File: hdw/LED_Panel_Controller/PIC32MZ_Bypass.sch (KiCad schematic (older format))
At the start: 14 parts

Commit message: added digikey pns, footprints, bom scrubbed
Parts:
- C? (x6): Digi-Key PN 490-13211-1-ND -> 1276-1451-1-ND
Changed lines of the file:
@@
 F 5 "6.3V" H 3090 3400 50  0000 R CNN "Voltage"
 F 6 "X5R" H 3090 3300 50  0000 R CNN "Dielectric"
-F 7 "490-13211-1-ND" H 3240 3400 50  0001 C CNN "Digi-Key PN"
+F 7 "1276-1451-1-ND" H 3240 3400 50  0001 C CNN "Digi-Key PN"
 	1    3240 3400
 	1    0    0    -1
@@
 F 5 "6.3V" H 4390 3400 50  0000 R CNN "Voltage"
 F 6 "X5R" H 4390 3300 50  0000 R CNN "Dielectric"
-F 7 "490-13211-1-ND" H 4540 3400 50  0001 C CNN "Digi-Key PN"
+F 7 "1276-1451-1-ND" H 4540 3400 50  0001 C CNN "Digi-Key PN"
 	1    4540 3400
 	1    0    0    -1
@@
 F 5 "6.3V" H 6990 3400 50  0000 R CNN "Voltage"
 F 6 "X5R" H 6990 3300 50  0000 R CNN "Dielectric"
-F 7 "490-13211-1-ND" H 7140 3400 50  0001 C CNN "Digi-Key PN"
+F 7 "1276-1451-1-ND" H 7140 3400 50  0001 C CNN "Digi-Key PN"
 	1    7140 3400
 	1    0    0    -1
@@
 F 5 "6.3V" H 5690 3400 50  0000 R CNN "Voltage"
 F 6 "X5R" H 5690 3300 50  0000 R CNN "Dielectric"
-F 7 "490-13211-1-ND" H 5840 3400 50  0001 C CNN "Digi-Key PN"
+F 7 "1276-1451-1-ND" H 5840 3400 50  0001 C CNN "Digi-Key PN"
 	1    5840 3400
 	1    0    0    -1
@@
 F 5 "6.3V" H 3090 4400 50  0000 R CNN "Voltage"
 F 6 "X5R" H 3090 4300 50  0000 R CNN "Dielectric"
-F 7 "490-13211-1-ND" H 3240 4400 50  0001 C CNN "Digi-Key PN"
+F 7 "1276-1451-1-ND" H 3240 4400 50  0001 C CNN "Digi-Key PN"
 	1    3240 4400
 	1    0    0    -1
@@
 F 5 "6.3V" H 6990 4400 50  0000 R CNN "Voltage"
 F 6 "X5R" H 6990 4300 50  0000 R CNN "Dielectric"
-F 7 "490-13211-1-ND" H 7140 4400 50  0001 C CNN "Digi-Key PN"
+F 7 "1276-1451-1-ND" H 7140 4400 50  0001 C CNN "Digi-Key PN"
 	1    7140 4400
 	1    0    0    -1

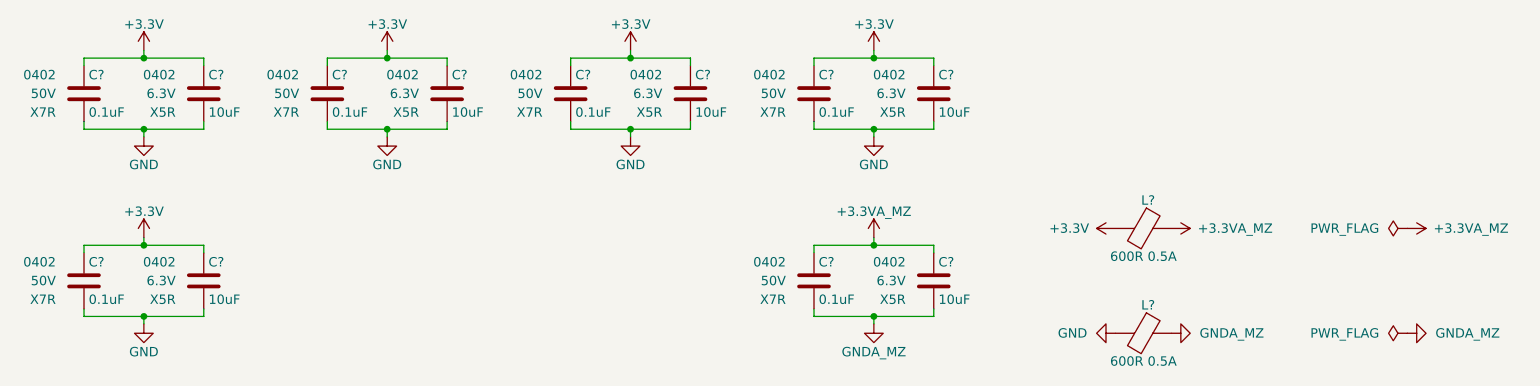
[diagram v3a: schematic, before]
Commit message: assigned I2C addresses
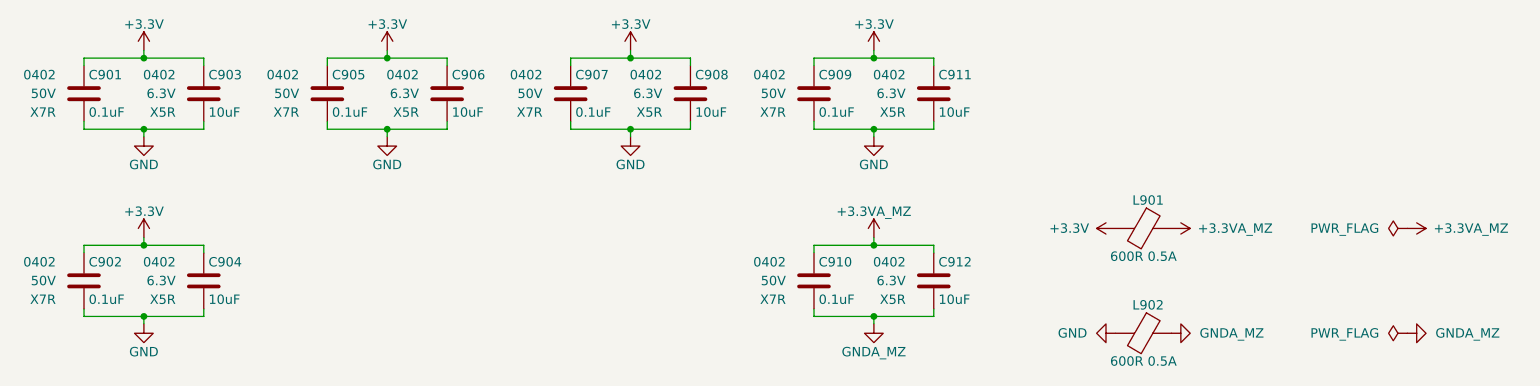
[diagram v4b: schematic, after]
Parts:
- gave numbers to parts that had none: 14
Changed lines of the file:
@@
 $EndDescr
 $Comp
-L Custom_Library:C_Custom C?
+L Custom_Library:C_Custom C901
 U 1 1 5CB29D37
 P 2600 3400
-F 0 "C?" H 2625 3500 50  0000 L CNN
+F 0 "C901" H 2625 3500 50  0000 L CNN
 F 1 "0.1uF" H 2625 3300 50  0000 L CNN
 F 2 "Capacitors_SMD:C_0402" H 2638 3250 50  0001 C CNN
@@
 	2600 3590 2600 3550
 $Comp
-L power:GND #PWR?
+L power:GND #PWR0906
 U 1 1 5CB1558B
 P 4220 3630
-F 0 "#PWR?" H 4220 3380 50  0001 C CNN
+F 0 "#PWR0906" H 4220 3380 50  0001 C CNN
 F 1 "GND" H 4220 3480 50  0000 C CNN
 F 2 "" H 4220 3630 50  0000 C CNN
@@
 $EndComp
 $Comp
-L Custom_Library:C_Custom C?
+L Custom_Library:C_Custom C905
 U 1 1 5CB15599
 P 3900 3400
-F 0 "C?" H 3925 3500 50  0000 L CNN
+F 0 "C905" H 3925 3500 50  0000 L CNN
 F 1 "0.1uF" H 3925 3300 50  0000 L CNN
 F 2 "Capacitors_SMD:C_0402" H 3938 3250 50  0001 C CNN
@@
 	4220 3590 4220 3630
 $Comp
-L power:GND #PWR?
+L power:GND #PWR0908
 U 1 1 5CB1993B
 P 5520 3630
-F 0 "#PWR?" H 5520 3380 50  0001 C CNN
+F 0 "#PWR0908" H 5520 3380 50  0001 C CNN
 F 1 "GND" H 5520 3480 50  0000 C CNN
 F 2 "" H 5520 3630 50  0000 C CNN
@@
 $EndComp
 $Comp
-L Custom_Library:C_Custom C?
+L Custom_Library:C_Custom C907
 U 1 1 5CB19945
 P 5200 3400
-F 0 "C?" H 5225 3500 50  0000 L CNN
+F 0 "C907" H 5225 3500 50  0000 L CNN
 F 1 "0.1uF" H 5225 3300 50  0000 L CNN
 F 2 "Capacitors_SMD:C_0402" H 5238 3250 50  0001 C CNN
@@
 	5520 3590 5520 3630
 $Comp
-L power:GND #PWR?
+L power:GND #PWR0910
 U 1 1 5CB219B2
 P 6820 3630
-F 0 "#PWR?" H 6820 3380 50  0001 C CNN
+F 0 "#PWR0910" H 6820 3380 50  0001 C CNN
 F 1 "GND" H 6820 3480 50  0000 C CNN
 F 2 "" H 6820 3630 50  0000 C CNN
@@
 $EndComp
 $Comp
-L Custom_Library:C_Custom C?
+L Custom_Library:C_Custom C909
 U 1 1 5CB219C0
 P 6500 3400
-F 0 "C?" H 6525 3500 50  0000 L CNN
+F 0 "C909" H 6525 3500 50  0000 L CNN
 F 1 "0.1uF" H 6525 3300 50  0000 L CNN
 F 2 "Capacitors_SMD:C_0402" H 6538 3250 50  0001 C CNN
@@
 	6820 3590 6820 3630
 $Comp
-L power:GND #PWR?
+L power:GND #PWR0904
 U 1 1 5CB24EB8
 P 2920 4630
-F 0 "#PWR?" H 2920 4380 50  0001 C CNN
+F 0 "#PWR0904" H 2920 4380 50  0001 C CNN
 F 1 "GND" H 2920 4480 50  0000 C CNN
 F 2 "" H 2920 4630 50  0000 C CNN
@@
 $EndComp
 $Comp
-L Custom_Library:C_Custom C?
+L Custom_Library:C_Custom C902
 U 1 1 5CB24EC6
 P 2600 4400
-F 0 "C?" H 2625 4500 50  0000 L CNN
+F 0 "C902" H 2625 4500 50  0000 L CNN
 F 1 "0.1uF" H 2625 4300 50  0000 L CNN
 F 2 "Capacitors_SMD:C_0402" H 2638 4250 50  0001 C CNN
@@
 	6500 4210 6500 4250
 $Comp
-L Custom_Library:C_Custom C?
+L Custom_Library:C_Custom C910
 U 1 1 5CB24FAA
 P 6500 4400
-F 0 "C?" H 6525 4500 50  0000 L CNN
+F 0 "C910" H 6525 4500 50  0000 L CNN
 F 1 "0.1uF" H 6525 4300 50  0000 L CNN
 F 2 "Capacitors_SMD:C_0402" H 6538 4250 50  0001 C CNN
@@
 AR Path="/5E697934/5CB5F840" Ref="L?"  Part="1"
 AR Path="/5EAE2F02/5CB5F840" Ref="L?"  Part="1"
-AR Path="/5F5829B3/5CB5F840" Ref="L?"  Part="1"
-F 0 "L?" V 8110 4145 50  0000 C CNN
+AR Path="/5F5829B3/5CB5F840" Ref="L901"  Part="1"
+F 0 "L901" V 8110 4145 50  0000 C CNN
 F 1 "600R 0.5A" V 8410 4120 50  0000 C CNN
 F 2 "Inductors_SMD:L_0402" V 8190 4120 50  0001 C CNN
@@
 AR Path="/5E697934/5CB61DC3" Ref="L?"  Part="1"
 AR Path="/5EAE2F02/5CB61DC3" Ref="L?"  Part="1"
-AR Path="/5F5829B3/5CB61DC3" Ref="L?"  Part="1"
-F 0 "L?" V 8110 4705 50  0000 C CNN
+AR Path="/5F5829B3/5CB61DC3" Ref="L902"  Part="1"
+F 0 "L902" V 8110 4705 50  0000 C CNN
 F 1 "600R 0.5A" V 8410 4680 50  0000 C CNN
 F 2 "Inductors_SMD:L_0402" V 8190 4680 50  0001 C CNN
@@
 $EndComp
 $Comp
-L power:GND #PWR?
+L power:GND #PWR0914
 U 1 1 5CB62D81
 P 8110 4680
-F 0 "#PWR?" H 8110 4430 50  0001 C CNN
+F 0 "#PWR0914" H 8110 4430 50  0001 C CNN
 F 1 "GND" V 8110 4530 50  0000 R CNN
 F 2 "" H 8110 4680 50  0001 C CNN
@@
 AR Path="/5E697934/5E325341" Ref="C?"  Part="1"
 AR Path="/5EAE2F02/5E325341" Ref="C?"  Part="1"
-AR Path="/5F5829B3/5E325341" Ref="C?"  Part="1"
-F 0 "C?" H 3265 3500 50  0000 L CNN
+AR Path="/5F5829B3/5E325341" Ref="C903"  Part="1"
+F 0 "C903" H 3265 3500 50  0000 L CNN
 F 1 "10uF" H 3265 3300 50  0000 L CNN
 F 2 "Capacitors_SMD:C_0402" H 3278 3250 50  0001 C CNN
@@
 AR Path="/5E697934/5E32800A" Ref="C?"  Part="1"
 AR Path="/5EAE2F02/5E32800A" Ref="C?"  Part="1"
-AR Path="/5F5829B3/5E32800A" Ref="C?"  Part="1"
-F 0 "C?" H 4565 3500 50  0000 L CNN
+AR Path="/5F5829B3/5E32800A" Ref="C906"  Part="1"
+F 0 "C906" H 4565 3500 50  0000 L CNN
 F 1 "10uF" H 4565 3300 50  0000 L CNN
 F 2 "Capacitors_SMD:C_0402" H 4578 3250 50  0001 C CNN
@@
 AR Path="/5E697934/5E32A559" Ref="C?"  Part="1"
 AR Path="/5EAE2F02/5E32A559" Ref="C?"  Part="1"
-AR Path="/5F5829B3/5E32A559" Ref="C?"  Part="1"
-F 0 "C?" H 7165 3500 50  0000 L CNN
+AR Path="/5F5829B3/5E32A559" Ref="C911"  Part="1"
+F 0 "C911" H 7165 3500 50  0000 L CNN
 F 1 "10uF" H 7165 3300 50  0000 L CNN
 F 2 "Capacitors_SMD:C_0402" H 7178 3250 50  0001 C CNN
@@
 $EndComp
 $Comp
-L power:PWR_FLAG #FLG?
+L power:PWR_FLAG #FLG0901
 U 1 1 5E44A219
 P 9670 4120
-F 0 "#FLG?" H 9670 4195 50  0001 C CNN
+F 0 "#FLG0901" H 9670 4195 50  0001 C CNN
 F 1 "PWR_FLAG" V 9670 4270 50  0000 L CNN
 F 2 "" H 9670 4120 50  0001 C CNN
@@
 $EndComp
 $Comp
-L power:PWR_FLAG #FLG?
+L power:PWR_FLAG #FLG0902
 U 1 1 5E44AB17
 P 9670 4680
-F 0 "#FLG?" H 9670 4755 50  0001 C CNN
+F 0 "#FLG0902" H 9670 4755 50  0001 C CNN
 F 1 "PWR_FLAG" V 9670 4830 50  0000 L CNN
 F 2 "" H 9670 4680 50  0001 C CNN
@@
 $EndComp
 $Comp
-L power:+3.3V #PWR?
+L power:+3.3V #PWR0909
 U 1 1 5E6E2CE4
 P 6820 3170
-F 0 "#PWR?" H 6820 3020 50  0001 C CNN
+F 0 "#PWR0909" H 6820 3020 50  0001 C CNN
 F 1 "+3.3V" H 6820 3310 50  0000 C CNN
 F 2 "" H 6820 3170 50  0001 C CNN
@@
 $EndComp
 $Comp
-L power:+3.3V #PWR?
+L power:+3.3V #PWR0907
 U 1 1 5E6E34DC
 P 5520 3170
-F 0 "#PWR?" H 5520 3020 50  0001 C CNN
+F 0 "#PWR0907" H 5520 3020 50  0001 C CNN
 F 1 "+3.3V" H 5520 3310 50  0000 C CNN
 F 2 "" H 5520 3170 50  0001 C CNN
@@
 $EndComp
 $Comp
-L power:+3.3V #PWR?
+L power:+3.3V #PWR0905
 U 1 1 5E6E3A94
 P 4220 3170
-F 0 "#PWR?" H 4220 3020 50  0001 C CNN
+F 0 "#PWR0905" H 4220 3020 50  0001 C CNN
 F 1 "+3.3V" H 4220 3310 50  0000 C CNN
 F 2 "" H 4220 3170 50  0001 C CNN
@@
 $EndComp
 $Comp
-L power:+3.3V #PWR?
+L power:+3.3V #PWR0903
 U 1 1 5E6E46E8
 P 2920 4170
-F 0 "#PWR?" H 2920 4020 50  0001 C CNN
+F 0 "#PWR0903" H 2920 4020 50  0001 C CNN
 F 1 "+3.3V" H 2920 4310 50  0000 C CNN
 F 2 "" H 2920 4170 50  0001 C CNN
@@
 $EndComp
 $Comp
-L power:+3.3V #PWR?
+L power:+3.3V #PWR0913
 U 1 1 5E6E6088
 P 8110 4120
-F 0 "#PWR?" H 8110 3970 50  0001 C CNN
+F 0 "#PWR0913" H 8110 3970 50  0001 C CNN
 F 1 "+3.3V" V 8110 4260 50  0000 L CNN
 F 2 "" H 8110 4120 50  0001 C CNN
@@
 $EndComp
 $Comp
-L Custom_Library:GNDA_MZ #PWR?
+L Custom_Library:GNDA_MZ #PWR0912
 U 1 1 5EB1572E
 P 6820 4630
-F 0 "#PWR?" H 6820 4380 50  0001 C CNN
+F 0 "#PWR0912" H 6820 4380 50  0001 C CNN
 F 1 "GNDA_MZ" H 6820 4480 50  0000 C CNN
 F 2 "" H 6820 4630 50  0001 C CNN
@@
 $EndComp
 $Comp
-L Custom_Library:GNDA_MZ #PWR?
+L Custom_Library:GNDA_MZ #PWR0916
 U 1 1 5EB160DB
 P 8410 4680
-F 0 "#PWR?" H 8410 4430 50  0001 C CNN
+F 0 "#PWR0916" H 8410 4430 50  0001 C CNN
 F 1 "GNDA_MZ" V 8410 4530 50  0000 R CNN
 F 2 "" H 8410 4680 50  0001 C CNN
@@
 $EndComp
 $Comp
-L Custom_Library:GNDA_MZ #PWR?
+L Custom_Library:GNDA_MZ #PWR0918
 U 1 1 5EB16842
 P 9670 4680
-F 0 "#PWR?" H 9670 4430 50  0001 C CNN
+F 0 "#PWR0918" H 9670 4430 50  0001 C CNN
 F 1 "GNDA_MZ" V 9670 4530 50  0000 R CNN
 F 2 "" H 9670 4680 50  0001 C CNN
@@
 $EndComp
 $Comp
-L Custom_Library:+3.3VA_MZ #PWR?
+L Custom_Library:+3.3VA_MZ #PWR0911
 U 1 1 5EB17B0F
 P 6820 4170
-F 0 "#PWR?" H 6820 4020 50  0001 C CNN
+F 0 "#PWR0911" H 6820 4020 50  0001 C CNN
 F 1 "+3.3VA_MZ" H 6820 4310 50  0000 C CNN
 F 2 "" H 6820 4170 50  0001 C CNN
@@
 $EndComp
 $Comp
-L Custom_Library:+3.3VA_MZ #PWR?
+L Custom_Library:+3.3VA_MZ #PWR0915
 U 1 1 5EB18347
 P 8410 4120
-F 0 "#PWR?" H 8410 3970 50  0001 C CNN
+F 0 "#PWR0915" H 8410 3970 50  0001 C CNN
 F 1 "+3.3VA_MZ" V 8410 4260 50  0000 L CNN
 F 2 "" H 8410 4120 50  0001 C CNN
@@
 $EndComp
 $Comp
-L Custom_Library:+3.3VA_MZ #PWR?
+L Custom_Library:+3.3VA_MZ #PWR0917
 U 1 1 5EB18B8A
 P 9670 4120
-F 0 "#PWR?" H 9670 3970 50  0001 C CNN
+F 0 "#PWR0917" H 9670 3970 50  0001 C CNN
 F 1 "+3.3VA_MZ" V 9670 4260 50  0000 L CNN
 F 2 "" H 9670 4120 50  0001 C CNN
@@
 $EndComp
 $Comp
-L power:+3.3V #PWR?
+L power:+3.3V #PWR0901
 U 1 1 5E6E4189
 P 2920 3170
-F 0 "#PWR?" H 2920 3020 50  0001 C CNN
+F 0 "#PWR0901" H 2920 3020 50  0001 C CNN
 F 1 "+3.3V" H 2920 3310 50  0000 C CNN
 F 2 "" H 2920 3170 50  0001 C CNN
@@
 Connection ~ 2920 3210
 $Comp
-L power:GND #PWR?
+L power:GND #PWR0902
 U 1 1 5CB29D2D
 P 2920 3630
-F 0 "#PWR?" H 2920 3380 50  0001 C CNN
+F 0 "#PWR0902" H 2920 3380 50  0001 C CNN
 F 1 "GND" H 2920 3480 50  0000 C CNN
 F 2 "" H 2920 3630 50  0000 C CNN
@@
 AR Path="/5E697934/5F6EBB55" Ref="C?"  Part="1"
 AR Path="/5EAE2F02/5F6EBB55" Ref="C?"  Part="1"
-AR Path="/5F5829B3/5F6EBB55" Ref="C?"  Part="1"
-F 0 "C?" H 5865 3500 50  0000 L CNN
+AR Path="/5F5829B3/5F6EBB55" Ref="C908"  Part="1"
+F 0 "C908" H 5865 3500 50  0000 L CNN
 F 1 "10uF" H 5865 3300 50  0000 L CNN
 F 2 "Capacitors_SMD:C_0402" H 5878 3250 50  0001 C CNN
@@
 AR Path="/5E697934/5F6F14C0" Ref="C?"  Part="1"
 AR Path="/5EAE2F02/5F6F14C0" Ref="C?"  Part="1"
-AR Path="/5F5829B3/5F6F14C0" Ref="C?"  Part="1"
-F 0 "C?" H 3265 4500 50  0000 L CNN
+AR Path="/5F5829B3/5F6F14C0" Ref="C904"  Part="1"
+F 0 "C904" H 3265 4500 50  0000 L CNN
 F 1 "10uF" H 3265 4300 50  0000 L CNN
 F 2 "Capacitors_SMD:C_0402" H 3278 4250 50  0001 C CNN
@@
 AR Path="/5E697934/5F6F395B" Ref="C?"  Part="1"
 AR Path="/5EAE2F02/5F6F395B" Ref="C?"  Part="1"
-AR Path="/5F5829B3/5F6F395B" Ref="C?"  Part="1"
-F 0 "C?" H 7165 4500 50  0000 L CNN
+AR Path="/5F5829B3/5F6F395B" Ref="C912"  Part="1"
+F 0 "C912" H 7165 4500 50  0000 L CNN
 F 1 "10uF" H 7165 4300 50  0000 L CNN
 F 2 "Capacitors_SMD:C_0402" H 7178 4250 50  0001 C CNN

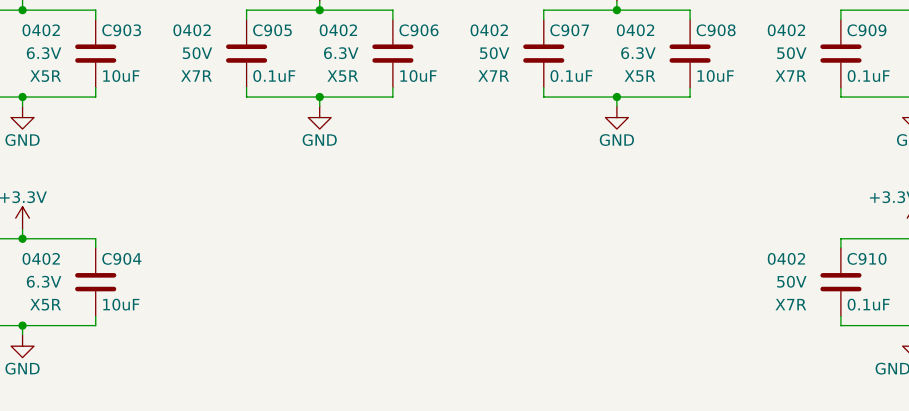
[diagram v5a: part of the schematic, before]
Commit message: separated function groups on PCB
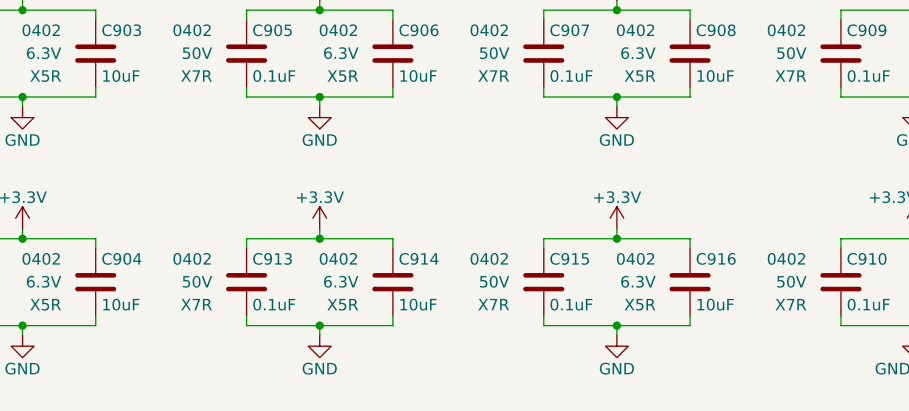
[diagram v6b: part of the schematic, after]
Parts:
- added C913, C915: 0.1uF, Capacitors_SMD:C_0402, symbol Custom_Library:C_Custom
- added C914, C916: 10uF, Capacitors_SMD:C_0402, symbol Custom_Library:C_Custom
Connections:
- net +3V3: now also C913.1, C914.1, C915.1, C916.1
- net GND: now also C913.2, C914.2, C915.2, C916.2
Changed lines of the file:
@@
 Wire Wire Line
 	6820 4590 7140 4590
+$Comp
+L power:GND #PWR0920
+U 1 1 60696CA9
+P 4220 4630
+F 0 "#PWR0920" H 4220 4380 50  0001 C CNN
+F 1 "GND" H 4220 4480 50  0000 C CNN
+F 2 "" H 4220 4630 50  0000 C CNN
+F 3 "" H 4220 4630 50  0000 C CNN
+	1    4220 4630
+	1    0    0    -1
+$EndComp
+$Comp
+L Custom_Library:C_Custom C913
+U 1 1 60696EDF
+P 3900 4400
+F 0 "C913" H 3925 4500 50  0000 L CNN
+F 1 "0.1uF" H 3925 4300 50  0000 L CNN
+F 2 "Capacitors_SMD:C_0402" H 3938 4250 50  0001 C CNN
+F 3 "" H 3925 4500 50  0001 C CNN
+F 4 "0402" H 3750 4500 50  0000 R CNN "display_footprint"
+F 5 "50V" H 3750 4400 50  0000 R CNN "Voltage"
+F 6 "X7R" H 3750 4300 50  0000 R CNN "Dielectric"
+F 7 "490-10701-1-ND" H -10 -2480 50  0001 C CNN "Digi-Key PN"
+	1    3900 4400
+	1    0    0    -1
+$EndComp
+Wire Wire Line
+	3900 4210 3900 4250
+Connection ~ 4220 4210
+Wire Wire Line
+	4540 4210 4540 4250
+Wire Wire Line
+	3900 4210 4220 4210
+Wire Wire Line
+	4220 4170 4220 4210
+Wire Wire Line
+	3900 4590 3900 4550
+Connection ~ 4220 4590
+Wire Wire Line
+	4540 4590 4540 4550
+Wire Wire Line
+	3900 4590 4220 4590
+Wire Wire Line
+	4220 4210 4540 4210
+Wire Wire Line
+	4220 4590 4540 4590
+Wire Wire Line
+	4220 4590 4220 4630
+$Comp
+L power:GND #PWR0922
+U 1 1 60696EF5
+P 5520 4630
+F 0 "#PWR0922" H 5520 4380 50  0001 C CNN
+F 1 "GND" H 5520 4480 50  0000 C CNN
+F 2 "" H 5520 4630 50  0000 C CNN
+F 3 "" H 5520 4630 50  0000 C CNN
+	1    5520 4630
+	1    0    0    -1
+$EndComp
+$Comp
+L Custom_Library:C_Custom C915
+U 1 1 60696F03
+P 5200 4400
+F 0 "C915" H 5225 4500 50  0000 L CNN
+F 1 "0.1uF" H 5225 4300 50  0000 L CNN
+F 2 "Capacitors_SMD:C_0402" H 5238 4250 50  0001 C CNN
+F 3 "" H 5225 4500 50  0001 C CNN
+F 4 "0402" H 5050 4500 50  0000 R CNN "display_footprint"
+F 5 "50V" H 5050 4400 50  0000 R CNN "Voltage"
+F 6 "X7R" H 5050 4300 50  0000 R CNN "Dielectric"
+F 7 "490-10701-1-ND" H 1290 -2480 50  0001 C CNN "Digi-Key PN"
+	1    5200 4400
+	1    0    0    -1
+$EndComp
+Wire Wire Line
+	5200 4210 5200 4250
+Wire Wire Line
+	5520 4170 5520 4210
+Wire Wire Line
+	5200 4590 5200 4550
+Wire Wire Line
+	5520 4590 5520 4630
+$Comp
+L Custom_Library:C_Custom C?
+U 1 1 60696F15
+P 4540 4400
+AR Path="/5CB7718D/60696F15" Ref="C?"  Part="1"
+AR Path="/5E0DC082/60696F15" Ref="C?"  Part="1"
+AR Path="/5E0F9110/60696F15" Ref="C?"  Part="1"
+AR Path="/5A557C58/60696F15" Ref="C?"  Part="1"
+AR Path="/5CB25152/60696F15" Ref="C?"  Part="1"
+AR Path="/5E697934/60696F15" Ref="C?"  Part="1"
+AR Path="/5EAE2F02/60696F15" Ref="C?"  Part="1"
+AR Path="/5F5829B3/60696F15" Ref="C914"  Part="1"
+F 0 "C914" H 4565 4500 50  0000 L CNN
+F 1 "10uF" H 4565 4300 50  0000 L CNN
+F 2 "Capacitors_SMD:C_0402" H 4578 4250 50  0001 C CNN
+F 3 "" H 4565 4500 50  0001 C CNN
+F 4 "0402" H 4390 4500 50  0000 R CNN "display_footprint"
+F 5 "6.3V" H 4390 4400 50  0000 R CNN "Voltage"
+F 6 "X5R" H 4390 4300 50  0000 R CNN "Dielectric"
+F 7 "1276-1451-1-ND" H 4540 4400 50  0001 C CNN "Digi-Key PN"
+	1    4540 4400
+	1    0    0    -1
+$EndComp
+$Comp
+L power:+3.3V #PWR0921
+U 1 1 60696F1F
+P 5520 4170
+F 0 "#PWR0921" H 5520 4020 50  0001 C CNN
+F 1 "+3.3V" H 5520 4310 50  0000 C CNN
+F 2 "" H 5520 4170 50  0001 C CNN
+F 3 "" H 5520 4170 50  0001 C CNN
+	1    5520 4170
+	1    0    0    -1
+$EndComp
+$Comp
+L power:+3.3V #PWR0919
+U 1 1 60696F29
+P 4220 4170
+F 0 "#PWR0919" H 4220 4020 50  0001 C CNN
+F 1 "+3.3V" H 4220 4310 50  0000 C CNN
+F 2 "" H 4220 4170 50  0001 C CNN
+F 3 "" H 4220 4170 50  0001 C CNN
+	1    4220 4170
+	1    0    0    -1
+$EndComp
+Wire Wire Line
+	5200 4210 5520 4210
+Wire Wire Line
+	5200 4590 5520 4590
+Connection ~ 5520 4210
+Wire Wire Line
+	5520 4210 5840 4210
+Connection ~ 5520 4590
+Wire Wire Line
+	5520 4590 5840 4590
+Wire Wire Line
+	5840 4210 5840 4250
+Wire Wire Line
+	5840 4590 5840 4550
+$Comp
+L Custom_Library:C_Custom C?
+U 1 1 60696F3F
+P 5840 4400
+AR Path="/5CB7718D/60696F3F" Ref="C?"  Part="1"
+AR Path="/5E0DC082/60696F3F" Ref="C?"  Part="1"
+AR Path="/5E0F9110/60696F3F" Ref="C?"  Part="1"
+AR Path="/5A557C58/60696F3F" Ref="C?"  Part="1"
+AR Path="/5CB25152/60696F3F" Ref="C?"  Part="1"
+AR Path="/5E697934/60696F3F" Ref="C?"  Part="1"
+AR Path="/5EAE2F02/60696F3F" Ref="C?"  Part="1"
+AR Path="/5F5829B3/60696F3F" Ref="C916"  Part="1"
+F 0 "C916" H 5865 4500 50  0000 L CNN
+F 1 "10uF" H 5865 4300 50  0000 L CNN
+F 2 "Capacitors_SMD:C_0402" H 5878 4250 50  0001 C CNN
+F 3 "" H 5865 4500 50  0001 C CNN
+F 4 "0402" H 5690 4500 50  0000 R CNN "display_footprint"
+F 5 "6.3V" H 5690 4400 50  0000 R CNN "Voltage"
+F 6 "X5R" H 5690 4300 50  0000 R CNN "Dielectric"
+F 7 "1276-1451-1-ND" H 5840 4400 50  0001 C CNN "Digi-Key PN"
+	1    5840 4400
+	1    0    0    -1
+$EndComp
 $EndSCHEMATC

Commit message: added BOMs, some consolidation
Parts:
- C901, C902, C905, C907, C909, C910, C913, C915: Digi-Key PN 490-10701-1-ND -> 490-10698-1-ND
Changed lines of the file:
@@
 F 5 "50V" H 2450 3400 50  0000 R CNN "Voltage"
 F 6 "X7R" H 2450 3300 50  0000 R CNN "Dielectric"
-F 7 "490-10701-1-ND" H -1310 -3480 50  0001 C CNN "Digi-Key PN"
+F 7 "490-10698-1-ND" H -1310 -3480 50  0001 C CNN "Digi-Key PN"
 	1    2600 3400
 	1    0    0    -1
@@
 F 5 "50V" H 3750 3400 50  0000 R CNN "Voltage"
 F 6 "X7R" H 3750 3300 50  0000 R CNN "Dielectric"
-F 7 "490-10701-1-ND" H -10 -3480 50  0001 C CNN "Digi-Key PN"
+F 7 "490-10698-1-ND" H -10 -3480 50  0001 C CNN "Digi-Key PN"
 	1    3900 3400
 	1    0    0    -1
@@
 F 5 "50V" H 5050 3400 50  0000 R CNN "Voltage"
 F 6 "X7R" H 5050 3300 50  0000 R CNN "Dielectric"
-F 7 "490-10701-1-ND" H 1290 -3480 50  0001 C CNN "Digi-Key PN"
+F 7 "490-10698-1-ND" H 1290 -3480 50  0001 C CNN "Digi-Key PN"
 	1    5200 3400
 	1    0    0    -1
@@
 F 5 "50V" H 6350 3400 50  0000 R CNN "Voltage"
 F 6 "X7R" H 6350 3300 50  0000 R CNN "Dielectric"
-F 7 "490-10701-1-ND" H 2590 -3480 50  0001 C CNN "Digi-Key PN"
+F 7 "490-10698-1-ND" H 2590 -3480 50  0001 C CNN "Digi-Key PN"
 	1    6500 3400
 	1    0    0    -1
@@
 F 5 "50V" H 2450 4400 50  0000 R CNN "Voltage"
 F 6 "X7R" H 2450 4300 50  0000 R CNN "Dielectric"
-F 7 "490-10701-1-ND" H -1310 -2480 50  0001 C CNN "Digi-Key PN"
+F 7 "490-10698-1-ND" H -1310 -2480 50  0001 C CNN "Digi-Key PN"
 	1    2600 4400
 	1    0    0    -1
@@
 F 5 "50V" H 6350 4400 50  0000 R CNN "Voltage"
 F 6 "X7R" H 6350 4300 50  0000 R CNN "Dielectric"
-F 7 "490-10701-1-ND" H 2590 -2480 50  0001 C CNN "Digi-Key PN"
+F 7 "490-10698-1-ND" H 2590 -2480 50  0001 C CNN "Digi-Key PN"
 	1    6500 4400
 	1    0    0    -1
@@
 F 5 "50V" H 3750 4400 50  0000 R CNN "Voltage"
 F 6 "X7R" H 3750 4300 50  0000 R CNN "Dielectric"
-F 7 "490-10701-1-ND" H -10 -2480 50  0001 C CNN "Digi-Key PN"
+F 7 "490-10698-1-ND" H -10 -2480 50  0001 C CNN "Digi-Key PN"
 	1    3900 4400
 	1    0    0    -1
@@
 F 5 "50V" H 5050 4400 50  0000 R CNN "Voltage"
 F 6 "X7R" H 5050 4300 50  0000 R CNN "Dielectric"
-F 7 "490-10701-1-ND" H 1290 -2480 50  0001 C CNN "Digi-Key PN"
+F 7 "490-10698-1-ND" H 1290 -2480 50  0001 C CNN "Digi-Key PN"
 	1    5200 4400
 	1    0    0    -1
